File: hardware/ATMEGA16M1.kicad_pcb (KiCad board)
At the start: 2 copper layers, 101.6 x 101.6 mm, 51 parts, among them IC1 ATMEGA16M1-A, IC2 MCP2551-I/SN, J1 PWR, J2 USB, J3 RELAY, J4 RELAY, J5 RELAY, J6 GPIO, J7 AMP/D2A, J8 ADC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

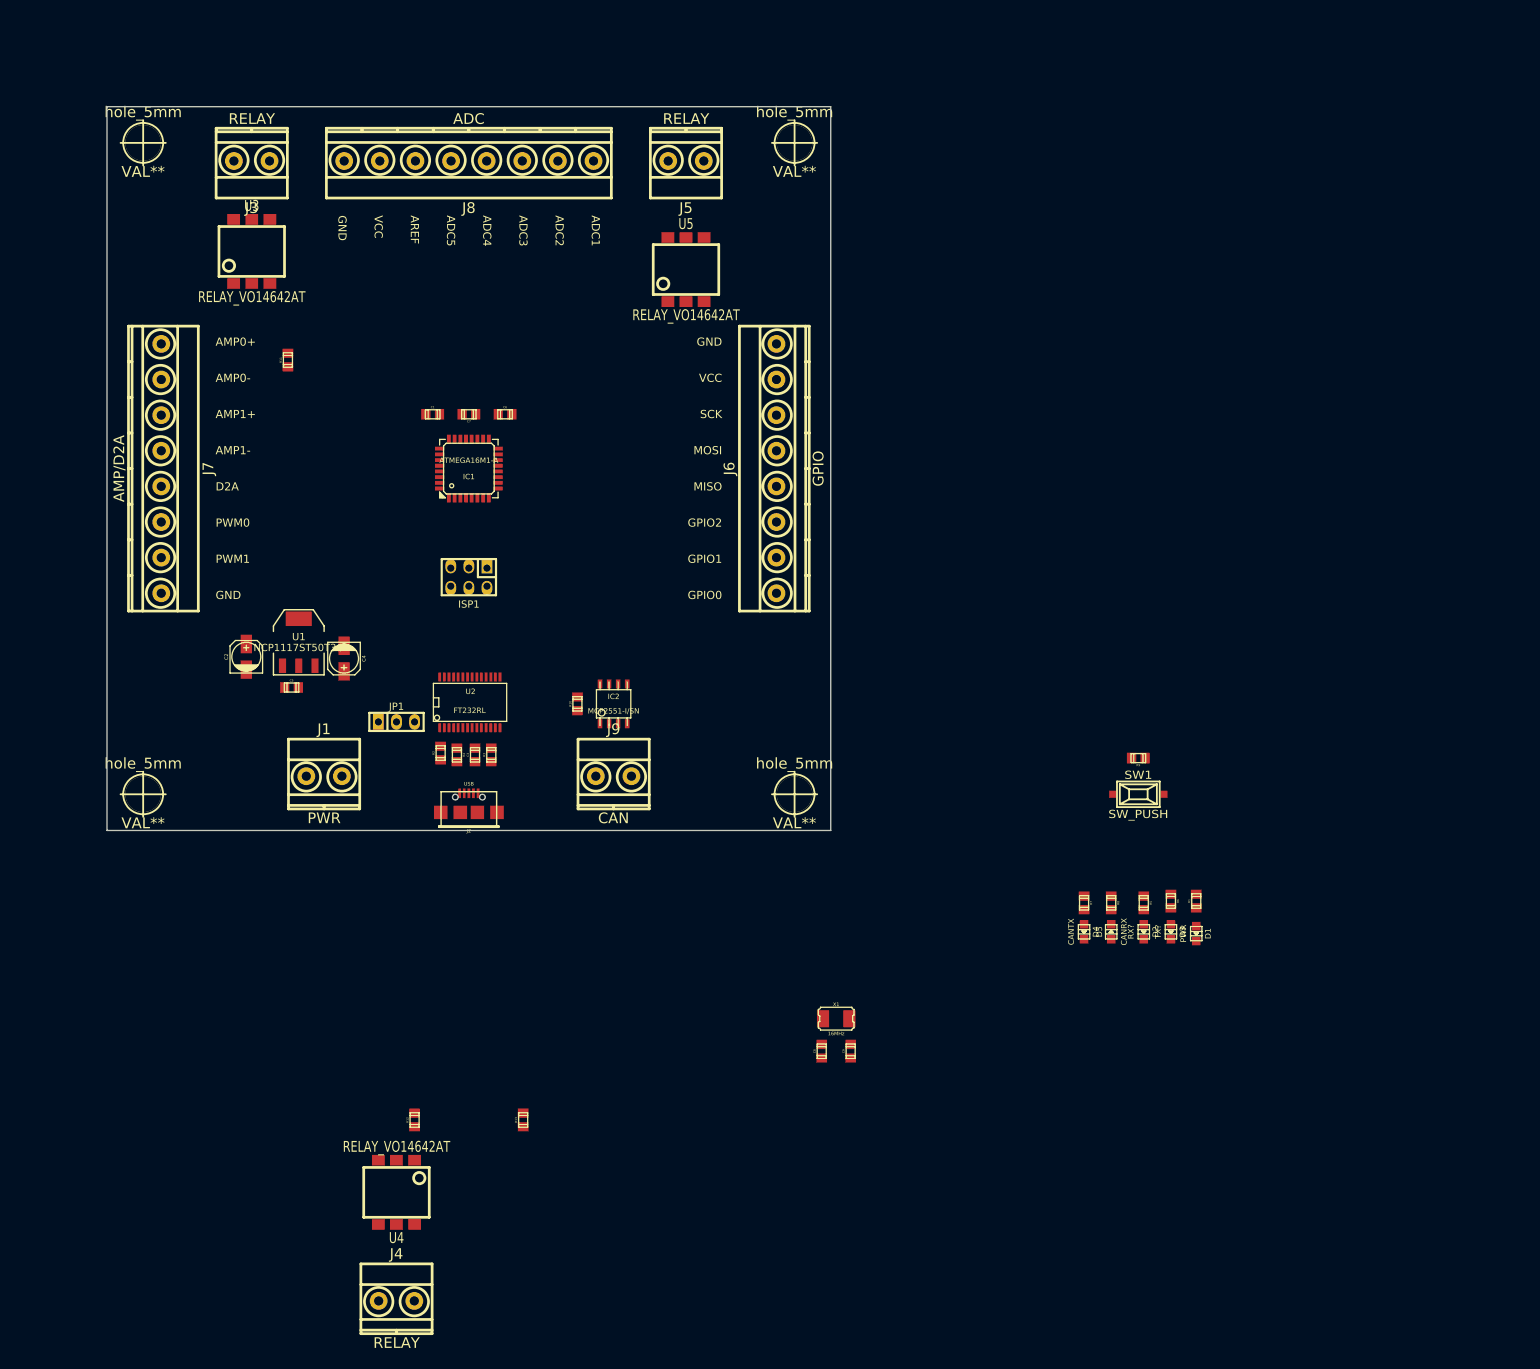
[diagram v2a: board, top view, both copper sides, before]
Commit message: PCB physical layout (mostly) complete
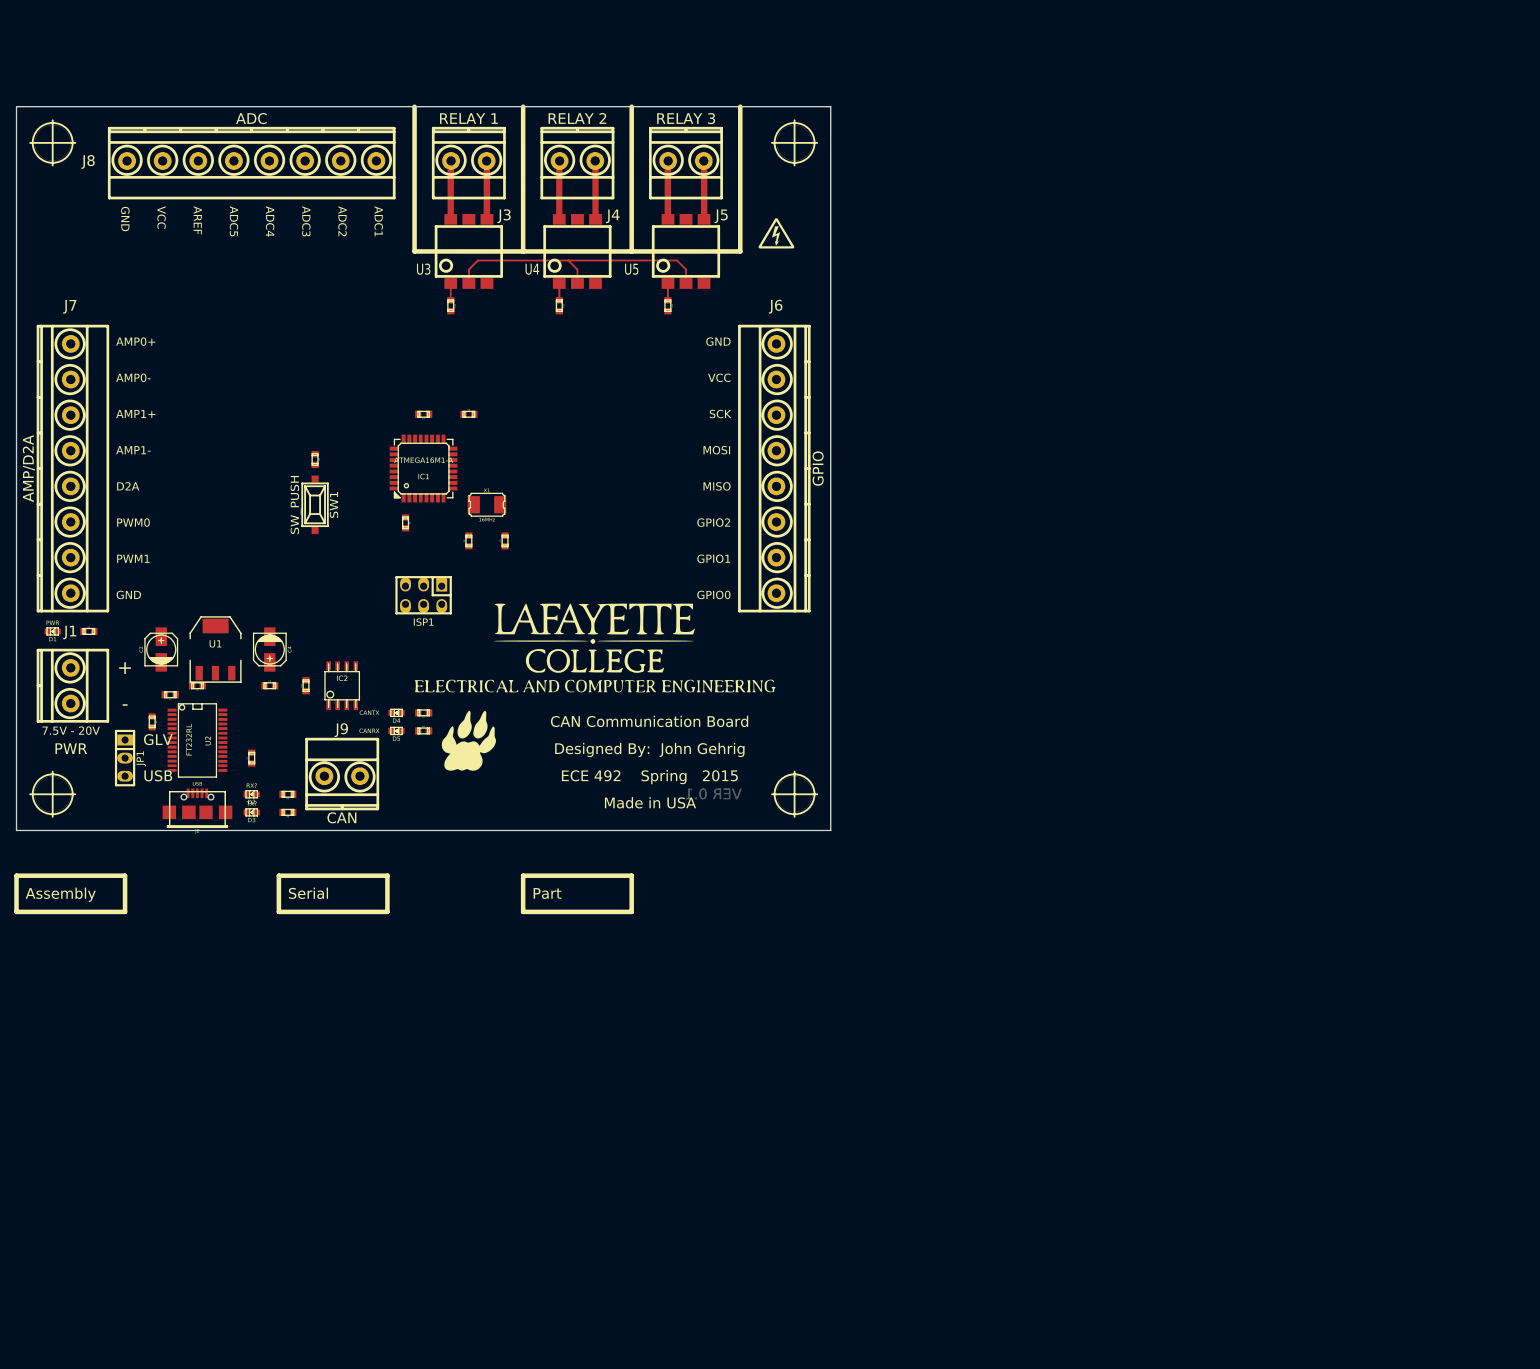
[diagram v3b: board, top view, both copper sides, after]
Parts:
- added G***: LOGO, Logo_silk_high_voltage_5x4.2mm, F.Cu at (149.9, 63.5)
- added G***: LEOPARD_PAW, LEOPARD_PAW, F.Cu at (106.7, 134.6)
- added G***: LAFAYETTE_ECE, LAFAYETTE_ECE, F.Cu at (124.5, 121.9)
- C1, C3, C5, C6, C7, C8, C9: footprint c_0805 -> c_0603
- D1, D2, D3, D4, D5: footprint Led_0805 -> Led_0603
- J3: value RELAY -> RELAY 1
- J4: value RELAY -> RELAY 2
- J5: value RELAY -> RELAY 3
- R1, R10, R11, R12, R13, R2, R3, R4, R5, R6, R7, R8, R9: footprint r_0805 -> r_0603
- moved D1 166.0 mm to (48.3, 119.4), turned to 180 degrees
- moved J4 162.0 mm to (121.9, 53.3), turned to 180 degrees
- moved R1 160.0 mm to (53.3, 119.4), turned to 0 degrees
- moved U4 134.5 mm to (121.9, 66.0), turned to 0 degrees
- moved D3 130.1 mm to (76.2, 144.8), turned to 180 degrees
- moved D2 126.7 mm to (76.2, 142.2), turned to 180 degrees
- moved R6 124.6 mm to (81.3, 144.8), turned to 180 degrees
- moved R9 122.9 mm to (85.1, 95.2), turned to 270 degrees
- moved SW1 122.5 mm to (85.1, 101.6), turned to 270 degrees
- moved R5 121.1 mm to (81.3, 142.2), turned to 180 degrees
- moved R12 116.1 mm to (119.4, 73.7), turned to 270 degrees
- moved R13 116.1 mm to (134.6, 73.7), turned to 270 degrees
- moved D5 104.2 mm to (96.5, 133.3), turned to 180 degrees
- moved D4 101.3 mm to (96.5, 130.8), turned to 180 degrees
- moved R8 99.5 mm to (100.3, 133.3), turned to 0 degrees
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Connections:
- U3 pad 4: /SSR_0B -> /SSR_0A
- U3 pad 6: /SSR_0A -> /SSR_0B
- U4 pad 4: /SSR_1B -> /SSR_1A
- U4 pad 6: /SSR_1A -> /SSR_1B
- U5 pad 4: /SSR_2B -> /SSR_2A
- U5 pad 6: /SSR_2A -> /SSR_2B
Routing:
- net GND: track 0.00 -> 39.2 mm
- net /SSR_1B: track 0.00 -> 8.22 mm
- net /SSR_0B: track 0.00 -> 8.22 mm
- net /SSR_2B: track 0.00 -> 8.22 mm
- net /SSR_2A: track 0.00 -> 8.21 mm
- net /SSR_1A: track 0.00 -> 8.21 mm
- net /SSR_0A: track 0.00 -> 8.21 mm
- net N-0000047: track 0.00 -> 2.36 mm
- net N-0000046: track 0.00 -> 2.36 mm
- net N-0000043: track 0.00 -> 2.36 mm
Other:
- board size 101.6 x 101.6 mm -> 114.3 x 101.6 mm
- net class HIGH_CURRENT added: clearance 0.381, trace_width 0.889, via_dia 1.143, via_drill 0.635
- board text added: "+"
- board text added: "-"
- board text added: "7.5V - 20V"
- board text added: "Assembly"
- board text added: "CAN Communication Board"
- board text added: "Designed By: John Gehrig"
- board text added: "ECE 492 Spring 2015"
- board text added: "GLV"
- board text added: "Made in USA"
- board text added: "Part"
- board text added: "Serial"
- board text added: "USB"
- board text added: "VER 0.1"

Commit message: PCB Prototype Finalized, GERBERs Created, Sent for Fabrication
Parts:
- removed the G*** at (106.7, 134.6)
- removed the G*** at (124.5, 121.9)
- added D10: DIODE, do214ac, F.Cu at (121.9, 61.6)
- added D11: DIODE, do214ac, F.Cu at (137.2, 61.6)
- added D6: RELAY1, LED-0603, F.Cu at (109.9, 77.5)
- added D7: RELAY2, LED-0603, F.Cu at (125.1, 77.5)
- added D8: RELAY3, LED-0603, F.Cu at (140.3, 77.5)
- added D9: DIODE, do214ac, F.Cu at (106.7, 61.6)
- added G***: LOGO, Logo_silk_ROHS_10x5.6mm, F.Cu at (112.4, 142.2)
- added G***: LOGO, Logo_silk_Lead-Free_5x5mm, F.Cu at (104.1, 142.2)
- added G***: lafayette_ece, lafayette_ece, F.Cu at (132.7, 124.5)
- added G***: lafayette_paw, lafayette_paw, F.Cu at (109.2, 131.4)
- added R14: 1k, r_0603, F.Cu at (109.9, 79.4)
- added R15: 1k, r_0603, F.Cu at (125.1, 79.4)
- added R16: 1k, r_0603, F.Cu at (140.3, 79.4)
- D2: value RX? -> RX
- D3: value TX? -> TX
- J3: value RELAY 1 -> RELAY1
- J4: value RELAY 2 -> RELAY2
- J5: value RELAY 3 -> RELAY3
- SW1: value SW_PUSH -> RESET
- moved R3 49.3 mm to (107.3, 96.5), turned to 0 degrees
- moved C3 41.3 mm to (93.5, 98.6)
- moved D1 30.2 mm to (78.1, 123.8)
- moved R1 28.3 mm to (81.3, 123.8)
- moved R9 17.8 mm to (85.1, 113.0), turned to 0 degrees
- moved C4 16.3 mm to (63.5, 116.2), turned to 90 degrees
- moved C6 15.8 mm to (100.3, 103.4), turned to 90 degrees
- moved C2 13.9 mm to (76.2, 116.2), turned to 270 degrees
- moved D3 13.5 mm to (78.1, 131.4), turned to 90 degrees
- moved C5 11.7 mm to (68.6, 121.3)
- moved D2 11.4 mm to (80.0, 131.4), turned to 90 degrees
- moved R6 10.6 mm to (78.1, 134.6), turned to 90 degrees
- moved R4 9.92 mm to (68.6, 124.5), turned to 0 degrees
- moved R10 8.98 mm to (92.7, 128.3), turned to 270 degrees
- moved SW1 8.26 mm to (85.1, 109.9), turned to 180 degrees
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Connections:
- IC1 pad 13: /ADC2 -> /ADC1
- IC1 pad 14: /ADC3 -> /ADC2
- IC1 pad 16: /ADC5 -> /GPIO0
- IC1 pad 26: /GPIO0 -> /ADC3
- IC1 pad 3: /PWM1 -> /PWM0
- ISP1 pad 3: /ADC1 -> /RXD
- J6 pad 1: /GPIO0 -> /MISO
- J6 pad 2: /GPIO1 -> /MOSI
- J6 pad 3: /GPIO2 -> /SCK
- J6 pad 4: /MISO -> /GPIO2
- J6 pad 5: /MOSI -> /GPIO1
- J6 pad 6: /SCK -> /GPIO0
- J7 pad 1: /AMP0+ -> /AMP0-
- J7 pad 2: /AMP0- -> /AMP0+
- J7 pad 3: /AMP1+ -> /AMP1-
- J7 pad 4: /AMP1- -> /AMP1+
- J7 pad 6: /MISO_A -> /PWM0
- J7 pad 7: /PWM1 -> /MISO_A
- J8 pad 1: /ADC1 -> /AREF
- J8 pad 2: /ADC2 -> GND
- J8 pad 3: /ADC3 -> /ADC1
- J8 pad 4: /ADC4 -> /ADC2
- J8 pad 5: /ADC5 -> /ADC3
- J8 pad 6: /AREF -> /ADC4
- J9 pad 1: /CAN_H -> /CAN_L
- J9 pad 2: /CAN_L -> /CAN_H
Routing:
- net VCC: track 0.00 -> 330.0 mm, vias 0 -> 1
- net GND: track 39.2 -> 160.8 mm, vias 0 -> 15
- net /ADC1: track 0.00 -> 74.5 mm, vias 0 -> 2
- net /ADC2: track 0.00 -> 73.7 mm, vias 0 -> 2
- net /SCK: track 0.00 -> 67.5 mm, vias 0 -> 2
- net /FTDI_RX: track 0.00 -> 67.3 mm, vias 0 -> 2
- net /MISO_A: track 0.00 -> 65.8 mm, vias 0 -> 3
- net /AMP1-: track 0.00 -> 57.5 mm, vias 0 -> 2
- net /ADC4: track 0.00 -> 56.7 mm, vias 0 -> 2
- net /GPIO2: track 0.00 -> 56.6 mm, vias 0 -> 2
- net /AMP1+: track 0.00 -> 55.3 mm, vias 0 -> 2
- net /SSR2: track 0.00 -> 54.7 mm, vias 0 -> 2
- net /MISO: track 0.00 -> 54.6 mm
- net /AMP0-: track 0.00 -> 54.2 mm
- net /CANRX: track 0.00 -> 54.1 mm
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- added copper zone on B.Cu, net GND
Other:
- net class Default: clearance 0.254 -> 0.1778
- net class POWER added: clearance 0.2032, trace_width 0.635, via_dia 1.143, via_drill 0.635
- rule trace_clearance: 0.254 -> 0.1778
- board text added: "+5V"
- board text added: "7.5V - 19V"
- board text added: "CAN_H"
- board text added: "CAN_L"
- board text added: "Made in the USA"
- board text added: "PWR SEL"
- board text added: "S/N"
- board text removed: "7.5V - 20V"
- board text removed: "ADC5"
- board text removed: "Assembly"
- board text removed: "Made in USA"
- board text removed: "Part"
- board text removed: "Serial"
- board text removed: "VCC"

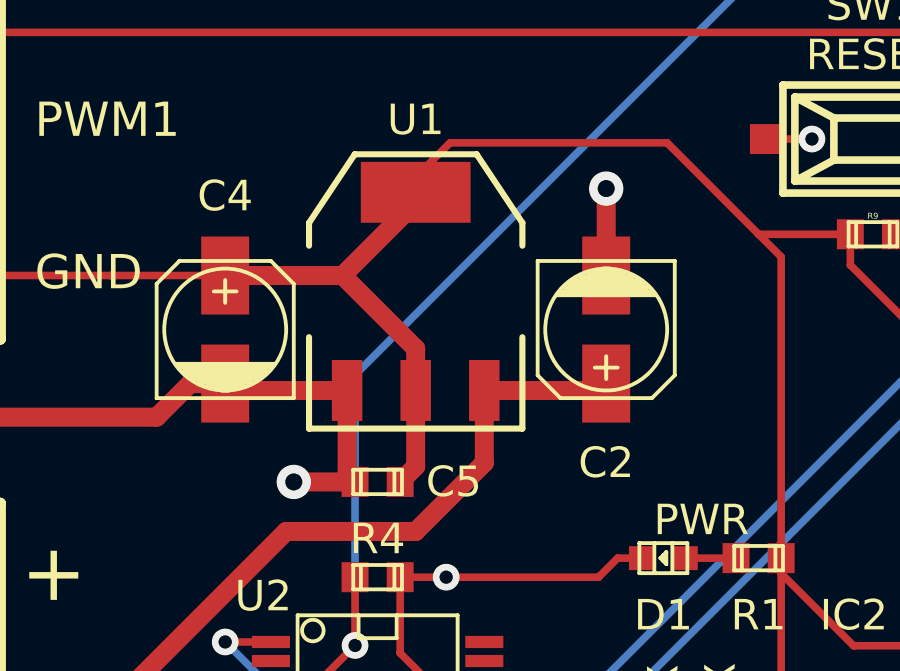
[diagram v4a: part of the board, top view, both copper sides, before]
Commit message: GERBER MODIFICATION (Annular Ring 5mil -> 10mil)
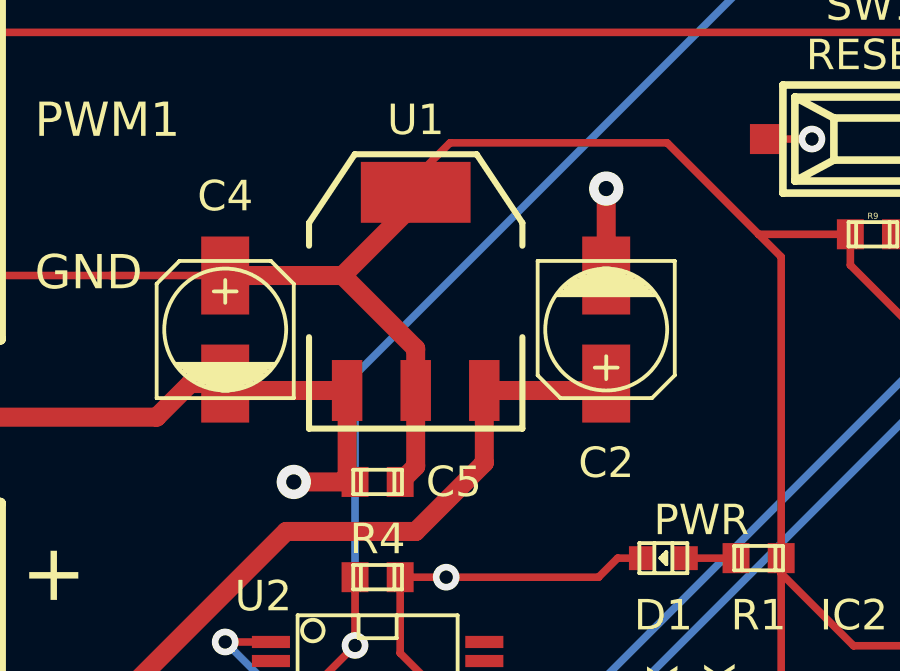
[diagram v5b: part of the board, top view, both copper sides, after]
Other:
- net class Default: via_drill 0.635 -> 0.508
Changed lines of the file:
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@@
 (kicad_pcb (version 3) (host pcbnew "(2013-may-18)-stable")
   (general
-    (links 0)
+    (links 134)
     (no_connects 0)
     (area 31.064288 35.250001 159.706733 147.5994)
@@
     (edge_width 0.1)
     (via_size 0.889)
-    (via_drill 0.635)
+    (via_drill 0.508)
     (via_min_size 0.889)
     (via_min_drill 0.508)
@@
     (trace_width 0.254)
     (via_dia 0.889)
-    (via_drill 0.635)
+    (via_drill 0.508)
     (uvia_dia 0.508)
     (uvia_drill 0.127)
@@
   (segment (start 96.52 113.03) (end 97.79 113.03) (width 0.254) (layer F.Cu) (net 44))
   (segment (start 89.408 109.855) (end 92.583 113.03) (width 0.254) (layer F.Cu) (net 44))
+  (via (at 121.92 76.2) (size 0.889) (layers F.Cu B.Cu) (net 45))
+  (via (at 137.16 76.2) (size 0.889) (layers F.Cu B.Cu) (net 45))
   (segment (start 139.5857 77.47) (end 138.43 77.47) (width 0.254) (layer F.Cu) (net 45))
   (segment (start 137.16 76.2) (end 137.16 74.35596) (width 0.254) (layer F.Cu) (net 45))
-  (via (at 137.16 76.2) (size 0.889) (layers F.Cu B.Cu) (net 45))
   (segment (start 138.43 77.47) (end 137.16 76.2) (width 0.254) (layer F.Cu) (net 45))
   (segment (start 124.3457 77.47) (end 123.19 77.47) (width 0.254) (layer F.Cu) (net 45))
   (segment (start 121.92 76.2) (end 121.92 74.35596) (width 0.254) (layer F.Cu) (net 45))
-  (via (at 121.92 76.2) (size 0.889) (layers F.Cu B.Cu) (net 45))
   (segment (start 123.19 77.47) (end 121.92 76.2) (width 0.254) (layer F.Cu) (net 45))
   (segment (start 109.1057 77.47) (end 107.95 77.47) (width 0.254) (layer F.Cu) (net 45))
